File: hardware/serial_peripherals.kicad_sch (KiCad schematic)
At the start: 10 parts, among them IC1 BMI270, IC2 SHT45-AD1F-R2, J1 Conn_01x04_Pin, U10 WSEN-PADS_2511020213301

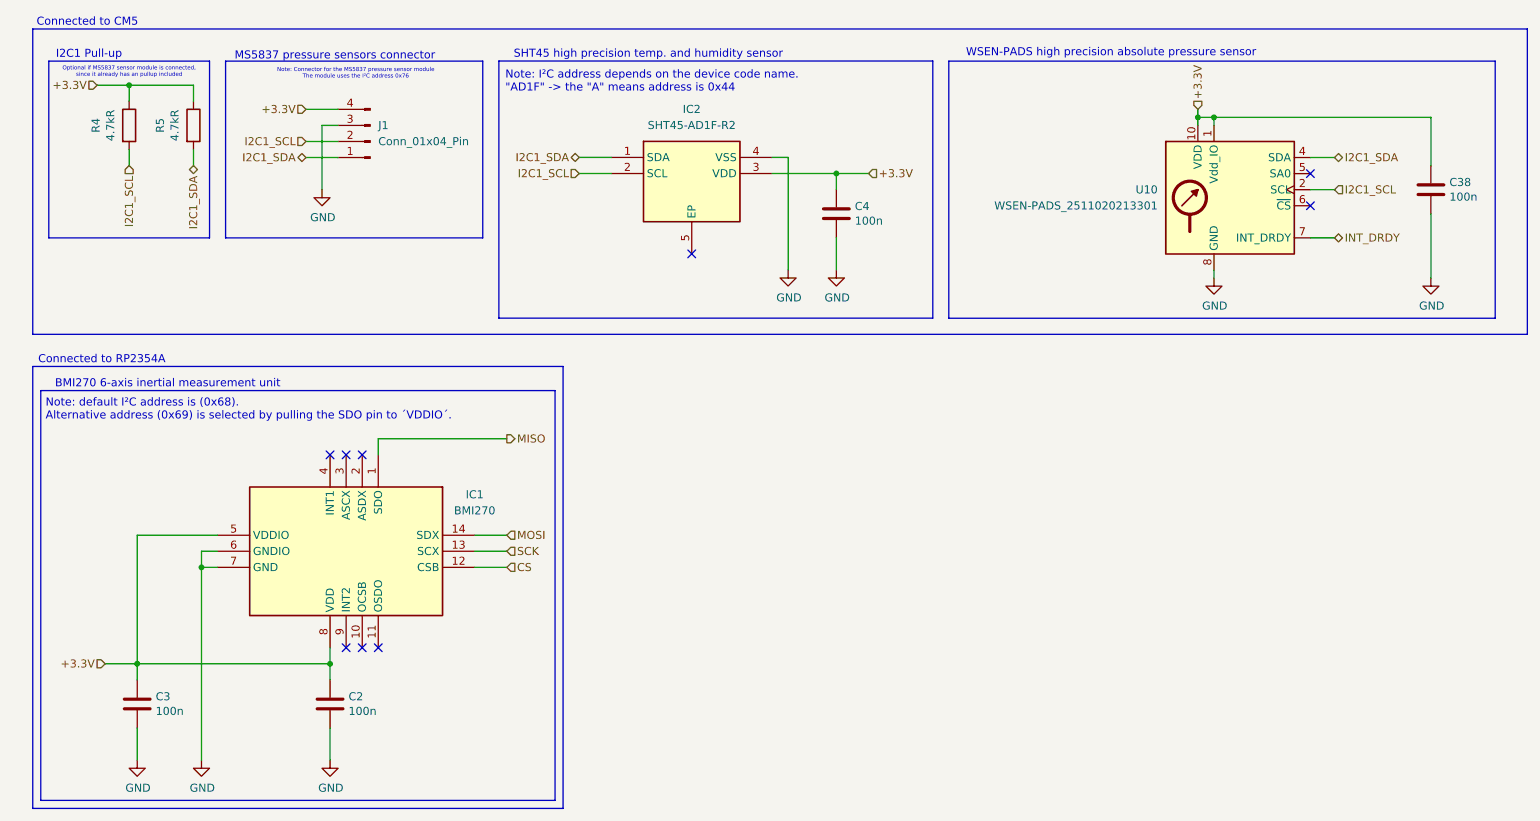
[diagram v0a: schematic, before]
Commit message: Add second camera, magnet load switch and schematic fixes
- Second camera J11 on MIPI1: I2C on ID_SD/ID_SC with 2.2k pull-ups,
  power enable on GPIO14/15 (CAM1_GPIO0/1); both cameras take 3.3 V
  from CM5_3.3V
- Magnet power switch: IC9 output is now +5V_AON, TPS22965 load switch
  IC15 drives +5V, J12 carries +5V_AON / MAG_ON / GND with R29
  pull-down; new TPS22965 symbol library
- Power: 4 A TPSM53604, 8 mOhm input sense resistor, C39/C40 bulk caps,
  F1-F3 battery polyfuses; 5 V raised to 5.115 V (R24 2.43k, 0.5 %
  feedback resistors); 47 uF at the CM5 5 V pins
- BMI270 on SPI and WSEN-PADS on I2C in serial_peripherals.kicad_sch
- Breakout headers J9/J13 with 5 V, 3.3 V and GND
- References renamed U -> IC; net classes for DPHY1, +5V, +5V_AON, +3.3V
- ERC clean (0 errors, 0 warnings); PCB update from the schematic is
  still in progress

Co-Authored-By: Claude Opus 5.5 <noreply@anthropic.com>
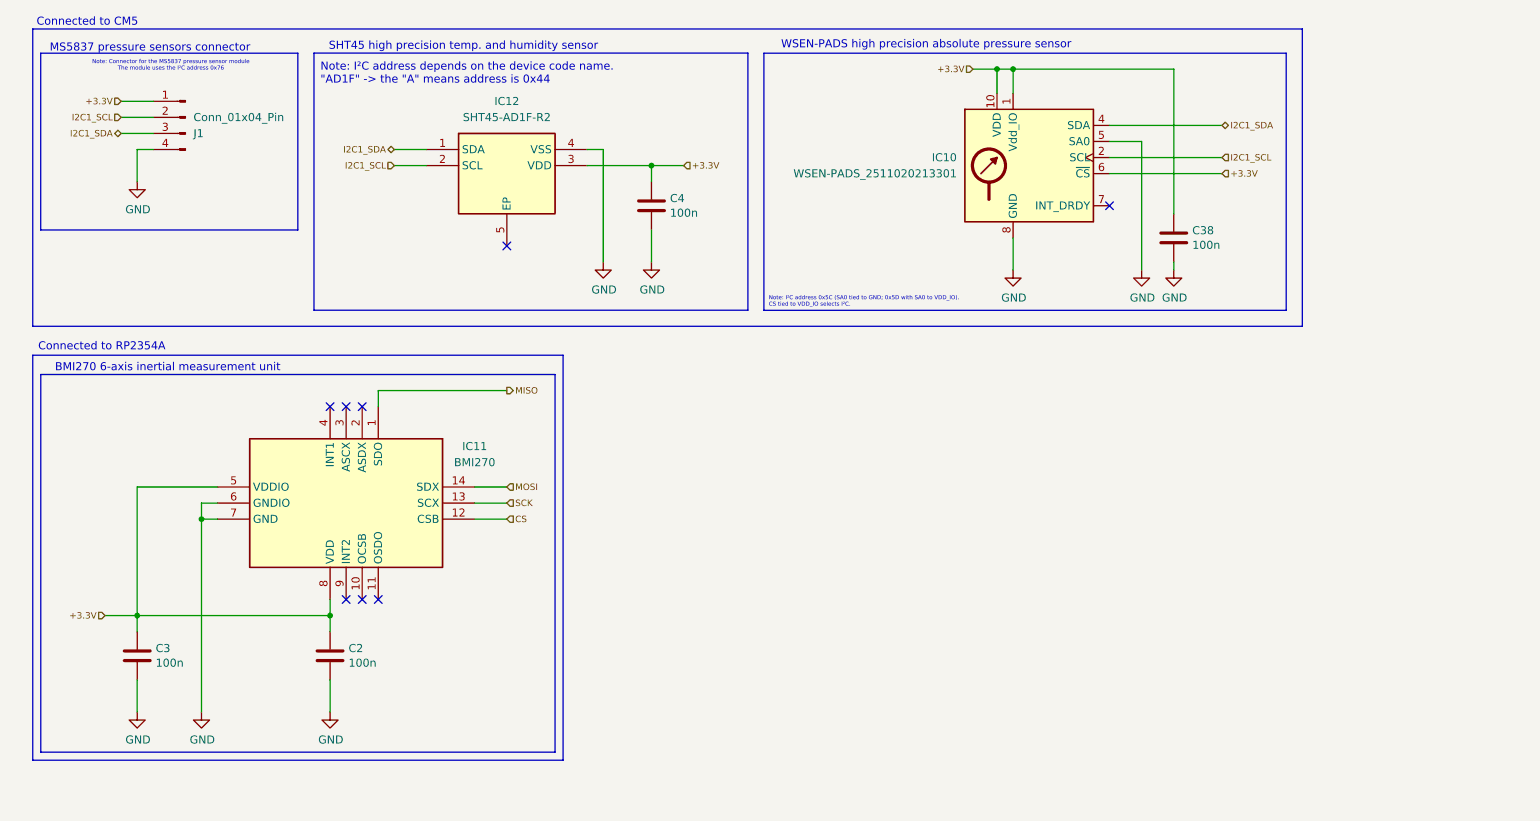
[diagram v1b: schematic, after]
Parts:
- removed R4, R5: 4.7kR, Resistor_SMD:R_0402_1005Metric, symbol Device:R
- IC10: renamed from U10; Mouser (none) -> https://mou.sr/3UkYI7Z; Mouser PN (none) -> 710-2511020213301
- renumbered IC1 to IC11, IC2 to IC12
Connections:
- net +3.3V: now also IC10.6 (~{CS}), J1.1 (Pin_1); no longer J1.4 (Pin_4)
- net GND: now also IC10.5 (SA0), J1.4 (Pin_4); no longer J1.3 (Pin_3)
- net I2C1_SDA: now also J1.3 (Pin_3); no longer J1.1 (Pin_1)
- net INT_DRDY: no longer names the net of IC10.7 (INT_DRDY)
- no-connect marks 9 -> 8
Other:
- note added: "Note: I²C address 0x5C (SA0 tied to GND; 0x5D with SA0 to VDD_IO). CS tied to VDD_IO selects I²C."
- note removed: "I2C1 Pull-up"
- note removed: "Note: default I²C address is (0x68). Alternative address (0x69) is selected by pulling the SDO pin to ´VDDIO´."
- note removed: "Optional if MS5837 sensor module is connected, since it already has an pullup included"
- moved on the sheet: C2, C3, C38, C4, IC10, IC11, IC12, J1

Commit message: Add LCSC part numbers and links, fix J7 part number
- Every part found on LCSC gets an "LCSC PN" (C-number) and an "LCSC" product
  link field, in the schematic and on the PCB footprints. Exact matches where
  LCSC lists the part; equivalents with the same specs where it does not or
  has no stock (C46, C26/C28/C30/C33/C34/C40, C29, C31, R6/R7, R21, R24,
  J3/J4, J7/J9/J13). Left empty: IC3, IC5 (not on LCSC), IC10, IC12
  (JLCPCB-only listings).
- J7: the MPN 61301421121 is a 2.54 mm header, but the footprint is 1.27 mm.
  Now Wurth 62201421121 (WR-PHD 1.27 mm 2x7) with matching description,
  datasheet and Mouser fields.
- Interactive HTML BOM in hardware/bom; KiCad project file re-saved.

Co-Authored-By: Claude Opus 5.5 <noreply@anthropic.com>
Claude-Session: https://claude.ai/code/session_01AhLYztcZikG9g81njGtEr1
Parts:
- C2, C3, C38, C4: LCSC (none) -> https://www.lcsc.com/product-detail/C71629.html; LCSC PN (none) -> C71629
- IC11: LCSC (none) -> https://www.lcsc.com/product-detail/C2836813.html; LCSC PN (none) -> C2836813
- J1: LCSC (none) -> https://www.lcsc.com/product-detail/C189895.html; LCSC PN (none) -> C189895
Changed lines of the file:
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@@
+			)
+		)
+		(property "LCSC PN" "C71629"
+			(at 113.03 45.72 0)
+			(hide yes)
+			(show_name no)
+			(do_not_autoplace no)
+			(effects
+				(font
+					(size 1.27 1.27)
+				)
+			)
+		)
+		(property "LCSC" "https://www.lcsc.com/product-detail/C71629.html"
+			(at 113.03 45.72 0)
+			(hide yes)
+			(show_name no)
+			(do_not_autoplace no)
+			(effects
+				(font
+					(size 1.27 1.27)
+				)
 			)
 		)
@@
 			)
 		)
+		(property "LCSC PN" "C189895"
+			(at 39.37 31.75 0)
+			(hide yes)
+			(show_name no)
+			(do_not_autoplace no)
+			(effects
+				(font
+					(size 1.27 1.27)
+				)
+			)
+		)
+		(property "LCSC" "https://www.lcsc.com/product-detail/C189895.html"
+			(at 39.37 31.75 0)
+			(hide yes)
+			(show_name no)
+			(do_not_autoplace no)
+			(effects
+				(font
+					(size 1.27 1.27)
+				)
+			)
+		)
 		(pin "4"
 		)
@@
 		)
 		(property "Mouser" "https://www.mouser.com/ProductDetail/81-GRM155R71C104KA88"
+			(at 31.75 116.84 0)
+			(hide yes)
+			(show_name no)
+			(do_not_autoplace no)
+			(effects
+				(font
+					(size 1.27 1.27)
+				)
+			)
+		)
+		(property "LCSC PN" "C71629"
+			(at 31.75 116.84 0)
+			(hide yes)
+			(show_name no)
+			(do_not_autoplace no)
+			(effects
+				(font
+					(size 1.27 1.27)
+				)
+			)
+		)
+		(property "LCSC" "https://www.lcsc.com/product-detail/C71629.html"
 			(at 31.75 116.84 0)
 			(hide yes)
@@
 			)
 		)
+		(property "LCSC PN" "C71629"
+			(at 195.58 50.8 0)
+			(hide yes)
+			(show_name no)
+			(do_not_autoplace no)
+			(effects
+				(font
+					(size 1.27 1.27)
+				)
+			)
+		)
+		(property "LCSC" "https://www.lcsc.com/product-detail/C71629.html"
+			(at 195.58 50.8 0)
+			(hide yes)
+			(show_name no)
+			(do_not_autoplace no)
+			(effects
+				(font
+					(size 1.27 1.27)
+				)
+			)
+		)
 		(pin "1"
 		)
@@
 		)
 		(property "Mouser" "https://www.mouser.com/ProductDetail/81-GRM155R71C104KA88"
+			(at 62.23 116.84 0)
+			(hide yes)
+			(show_name no)
+			(do_not_autoplace no)
+			(effects
+				(font
+					(size 1.27 1.27)
+				)
+			)
+		)
+		(property "LCSC PN" "C71629"
+			(at 62.23 116.84 0)
+			(hide yes)
+			(show_name no)
+			(do_not_autoplace no)
+			(effects
+				(font
+					(size 1.27 1.27)
+				)
+			)
+		)
+		(property "LCSC" "https://www.lcsc.com/product-detail/C71629.html"
 			(at 62.23 116.84 0)
 			(hide yes)
@@
 			(at 69.85 77.47 0)
 			(hide yes)
+			(show_name no)
+			(do_not_autoplace no)
+			(effects
+				(font
+					(size 1.27 1.27)
+				)
+			)
+		)
+		(property "LCSC PN" "C2836813"
+			(at 69.85 77.47 0)
+			(hide yes)
+			(show_name no)
+			(do_not_autoplace no)
+			(effects
+				(font
+					(size 1.27 1.27)
+				)
+			)
+		)
+		(property "LCSC" "https://www.lcsc.com/product-detail/C2836813.html"
+			(at 69.85 77.47 0)
+			(hide yes)
